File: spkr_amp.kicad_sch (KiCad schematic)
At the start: 6 parts, among them U2 TPA2006D1DRBR

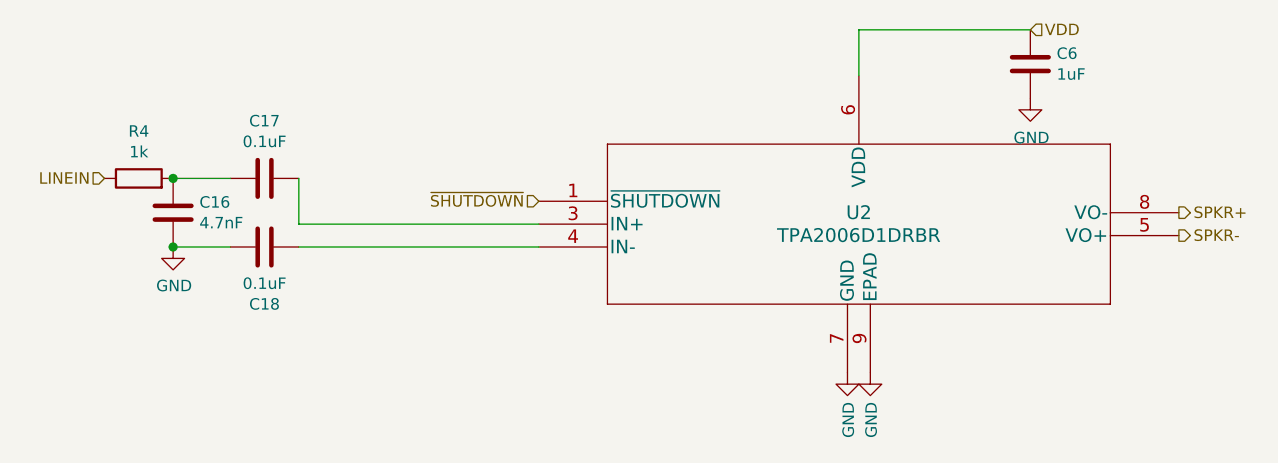
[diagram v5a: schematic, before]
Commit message: Start re-routing CM4 board with most parts on the back layer, and CM4 itself turned around so that the BCM2711 is in a deeper part of the iPad case.
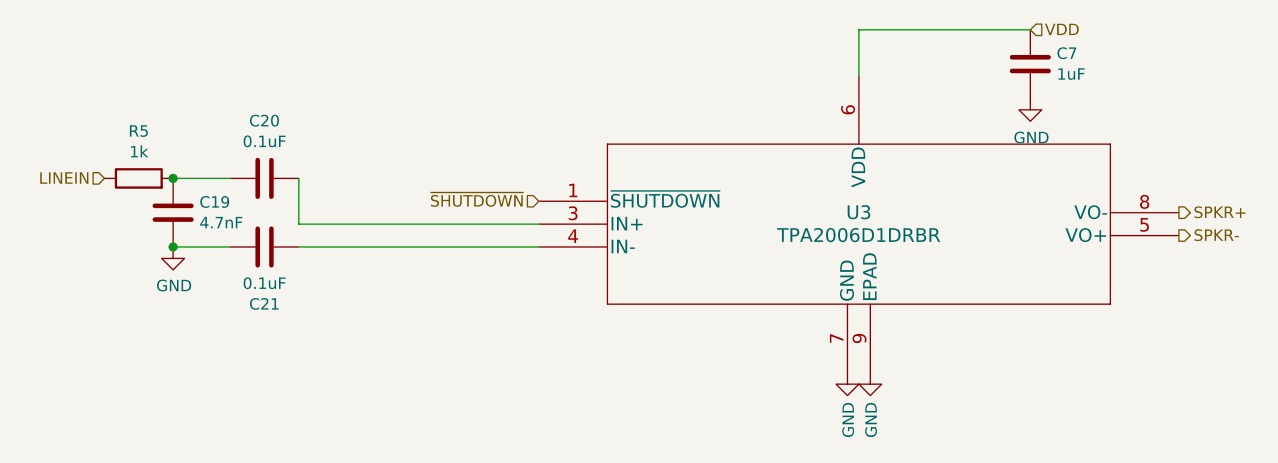
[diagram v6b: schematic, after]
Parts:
- renumbered C16 to C19, C17 to C20, C18 to C21, C6 to C7, R4 to R5, U2 to U3
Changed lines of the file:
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@@
   (symbol (lib_id "Device:C") (at 190.5 66.04 0)
     (in_bom yes) (on_board yes)
-    (property "Reference" "C6" (id 0) (at 193.421 64.8716 0)
+    (property "Reference" "C7" (id 0) (at 193.421 64.8716 0)
       (effects (font (size 1.27 1.27)) (justify left))
     )
@@
   (symbol (lib_id "TPA2006D1DRBR:TPA2006D1DRBR") (at 171.45 83.82 0)
     (in_bom yes) (on_board yes)
-    (property "Reference" "U2" (id 0) (at 171.45 82.55 0)
+    (property "Reference" "U3" (id 0) (at 171.45 82.55 0)
       (effects (font (size 1.524 1.524)))
     )
@@
   (symbol (lib_id "Device:C") (at 105.41 78.74 90)
     (in_bom yes) (on_board yes)
-    (property "Reference" "C17" (id 0) (at 105.41 72.3708 90))
+    (property "Reference" "C20" (id 0) (at 105.41 72.3708 90))
     (property "Value" "0.1uF" (id 1) (at 105.41 74.669 90))
     (property "Footprint" "Capacitor_SMD:C_0402_1005Metric" (id 2) (at 109.22 77.7748 0)
@@
   (symbol (lib_id "Device:R") (at 91.44 78.74 90)
     (in_bom yes) (on_board yes)
-    (property "Reference" "R4" (id 0) (at 91.44 73.5138 90))
+    (property "Reference" "R5" (id 0) (at 91.44 73.5138 90))
     (property "Value" "1k" (id 1) (at 91.44 75.812 90))
     (property "Footprint" "Resistor_SMD:R_0402_1005Metric" (id 2) (at 91.44 80.518 90)
@@
   (symbol (lib_id "Device:C") (at 105.41 86.36 90)
     (in_bom yes) (on_board yes)
-    (property "Reference" "C18" (id 0) (at 105.41 92.7292 90))
+    (property "Reference" "C21" (id 0) (at 105.41 92.7292 90))
     (property "Value" "0.1uF" (id 1) (at 105.41 90.43 90))
     (property "Footprint" "Capacitor_SMD:C_0402_1005Metric" (id 2) (at 109.22 85.3948 0)
@@
   (symbol (lib_id "Device:C") (at 95.25 82.55 0)
     (in_bom yes) (on_board yes)
-    (property "Reference" "C16" (id 0) (at 98.1711 81.4006 0)
+    (property "Reference" "C19" (id 0) (at 98.1711 81.4006 0)
       (effects (font (size 1.27 1.27)) (justify left))
     )

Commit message: Adjust edge cuts to make room for LVDS cable to come up. Adjust TPA2006 footprint to allow PAM8320AASCR (MSOP-8) to fit also; adjust board to compensate for this larger footprint. Fix some silkscreen issues.
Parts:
- U3: footprint footprints:TPA2006D1DRBR -> footprints:TPA2006_PAM8302
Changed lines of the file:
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@@
   (symbol (lib_id "power:GND") (at 190.5 69.85 0)
     (in_bom yes) (on_board yes)
-    (property "Reference" "#PWR0118" (id 0) (at 190.5 76.2 0)
+    (property "Reference" "#PWR0110" (id 0) (at 190.5 76.2 0)
       (effects (font (size 1.27 1.27)) hide)
     )
@@
   (symbol (lib_id "power:GND") (at 170.18 100.33 0)
     (in_bom yes) (on_board yes)
-    (property "Reference" "#PWR0116" (id 0) (at 170.18 106.68 0)
+    (property "Reference" "#PWR0107" (id 0) (at 170.18 106.68 0)
       (effects (font (size 1.27 1.27)) hide)
     )
@@
   (symbol (lib_id "power:GND") (at 172.72 100.33 0)
     (in_bom yes) (on_board yes)
-    (property "Reference" "#PWR0117" (id 0) (at 172.72 106.68 0)
+    (property "Reference" "#PWR0108" (id 0) (at 172.72 106.68 0)
       (effects (font (size 1.27 1.27)) hide)
     )
@@
       (effects (font (size 1.524 1.524)))
     )
-    (property "Footprint" "footprints:TPA2006D1DRBR" (id 2) (at 207.01 77.724 0)
+    (property "Footprint" "footprints:TPA2006_PAM8302" (id 2) (at 207.01 77.724 0)
       (effects (font (size 1.524 1.524)) hide)
     )
@@
   (symbol (lib_id "power:GND") (at 95.25 86.36 0)
     (in_bom yes) (on_board yes)
-    (property "Reference" "#PWR0112" (id 0) (at 95.25 92.71 0)
+    (property "Reference" "#PWR0105" (id 0) (at 95.25 92.71 0)
       (effects (font (size 1.27 1.27)) hide)
     )
